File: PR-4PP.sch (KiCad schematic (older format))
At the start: 14 parts

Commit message: sch & pcb changes
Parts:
- added D1, D2, D3, D4: D_Small, Diode_SMD:D_SOD-123, symbol Device:D_Small
- added F1: 500mA, Fuse:Fuse_1206_3216Metric, symbol Device:Polyfuse
- added MX1, MX2, MX3: MX-NoLED, MX_Alps_Hybrid:MX-1U-NoLED, symbol MX_Alps_Hybrid:MX-NoLED
- added MX4: MX-NoLED, MX_Alps_Hybrid:MX-1U, symbol MX_Alps_Hybrid:MX-NoLED
- added USB1: Molex-0548190589, random-keyboard-parts:Molex-0548190589, symbol random-keyboard-parts:Molex-0548190589
- C1, C2, C3, C4, C5, C6, C7: renamed from C?; footprint (none) -> Capacitor_SMD:C_0805_2012Metric
- R1, R2, R3, R4: renamed from R?; footprint (none) -> Resistor_SMD:R_0805_2012Metric
- SW1: renamed from SW?; footprint (none) -> random-keyboard-parts:SKQG-1155865
- Y1: renamed from Y?; footprint (none) -> Crystal:Crystal_SMD_3225-4Pin_3.2x2.5mm
- gave numbers to parts that had none: 1
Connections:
- net +5V: now also F1.1
- net D+: now also USB1.3 (D+)
- net D-: now also USB1.4 (D-)
- net GND: now also USB1.1 (GND)
- new net: D1.2 (A), MX1.2 (ROW)
- new net: D3.2 (A), MX3.2 (ROW)
- new net: D2.2 (A), MX2.2 (ROW)
- new net: D4.2 (A), MX4.2 (ROW)
- new net COL0: MX1.1 (COL), MX3.1 (COL)
- new net COL1: MX2.1 (COL), MX4.1 (COL)
- new net ROW0: D1.1 (K), D2.1 (K)
- new net ROW1: D3.1 (K), D4.1 (K)
- new net VCC: F1.2, USB1.5 (VBUS)
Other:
- moved on the sheet: C1, C2, C3, C4, C5, C6, C7, R1, R2, R3, R4, SW1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

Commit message: finish pcb
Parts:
- renumbered C5 to C1, C7 to C3, C1 to C4, C2 to C5, C3 to C6, C4 to C7, R3 to R1, R1 to R3, C6 to c2
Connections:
- net COL0: now also U1.29 (PB5)
- net COL1: now also U1.28 (PB4)
- net ROW0: now also U1.27 (PD7)
- net ROW1: now also U1.30 (PB6)
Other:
- moved on the sheet: R4
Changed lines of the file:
@@
 L Device:R_Small R4
 U 1 1 6167D378
-P 5300 4850
-F 0 "R4" V 5104 4850 50  0000 C CNN
-F 1 "10k" V 5195 4850 50  0000 C CNN
-F 2 "Resistor_SMD:R_0805_2012Metric" H 5300 4850 50  0001 C CNN
-F 3 "~" H 5300 4850 50  0001 C CNN
-	1    5300 4850
-	0    1    1    0
-$EndComp
-Wire Wire Line
-	5200 4850 5000 4850
+P 5450 4850
+F 0 "R4" V 5254 4850 50  0000 C CNN
+F 1 "10k" V 5345 4850 50  0000 C CNN
+F 2 "Resistor_SMD:R_0805_2012Metric" H 5450 4850 50  0001 C CNN
+F 3 "~" H 5450 4850 50  0001 C CNN
+	1    5450 4850
+	0    1    1    0
+$EndComp
+Wire Wire Line
+	5350 4850 5000 4850
 $Comp
 L power:GND #PWR0103
@@
 $EndComp
 Wire Wire Line
-	5400 4850 5750 4850
+	5550 4850 5750 4850
 $Comp
 L Device:R_Small R2
@@
 $EndComp
 $Comp
-L Device:R_Small R1
+L Device:R_Small R3
 U 1 1 6167ECE6
 P 2900 3850
-F 0 "R1" V 2704 3850 50  0000 C CNN
+F 0 "R3" V 2704 3850 50  0000 C CNN
 F 1 "22" V 2795 3850 50  0000 C CNN
 F 2 "Resistor_SMD:R_0805_2012Metric" H 2900 3850 50  0001 C CNN
@@
 	3800 3750 3250 3750
 $Comp
-L Device:C_Small C7
+L Device:C_Small C3
 U 1 1 61680FED
 P 3150 4150
-F 0 "C7" H 3058 4104 50  0000 R CNN
+F 0 "C3" H 3058 4104 50  0000 R CNN
 F 1 "1uF" H 3058 4195 50  0000 R CNN
 F 2 "Capacitor_SMD:C_0805_2012Metric" H 3150 4150 50  0001 C CNN
@@
 	3150 4250 3150 4450
 $Comp
-L Device:C_Small C1
+L Device:C_Small C4
 U 1 1 616827A2
 P 1350 5100
-F 0 "C1" H 1442 5146 50  0000 L CNN
+F 0 "C4" H 1442 5146 50  0000 L CNN
 F 1 "0.1uF" H 1442 5055 50  0000 L CNN
 F 2 "Capacitor_SMD:C_0805_2012Metric" H 1350 5100 50  0001 C CNN
@@
 $EndComp
 $Comp
-L Device:C_Small C2
+L Device:C_Small C5
 U 1 1 61683F91
 P 1800 5100
-F 0 "C2" H 1892 5146 50  0000 L CNN
+F 0 "C5" H 1892 5146 50  0000 L CNN
 F 1 "0.1uF" H 1892 5055 50  0000 L CNN
 F 2 "Capacitor_SMD:C_0805_2012Metric" H 1800 5100 50  0001 C CNN
@@
 $EndComp
 $Comp
-L Device:C_Small C3
+L Device:C_Small C6
 U 1 1 616845F6
 P 2250 5100
-F 0 "C3" H 2342 5146 50  0000 L CNN
+F 0 "C6" H 2342 5146 50  0000 L CNN
 F 1 "0.1uF" H 2342 5055 50  0000 L CNN
 F 2 "Capacitor_SMD:C_0805_2012Metric" H 2250 5100 50  0001 C CNN
@@
 $EndComp
 $Comp
-L Device:C_Small C4
+L Device:C_Small C7
 U 1 1 61684895
 P 2700 5100
-F 0 "C4" H 2792 5146 50  0000 L CNN
+F 0 "C7" H 2792 5146 50  0000 L CNN
 F 1 "10uF" H 2792 5055 50  0000 L CNN
 F 2 "Capacitor_SMD:C_0805_2012Metric" H 2700 5100 50  0001 C CNN
@@
 	3800 3150 3200 3150
 $Comp
-L Device:C_Small C5
+L Device:C_Small C1
 U 1 1 61689DB9
 P 2750 2850
-F 0 "C5" V 2521 2850 50  0000 C CNN
+F 0 "C1" V 2521 2850 50  0000 C CNN
 F 1 "22pF" V 2612 2850 50  0000 C CNN
 F 2 "Capacitor_SMD:C_0805_2012Metric" H 2750 2850 50  0001 C CNN
@@
 $EndComp
 $Comp
-L Device:C_Small C6
+L Device:C_Small c2
 U 1 1 6168B87D
 P 2750 3250
-F 0 "C6" V 2521 3250 50  0000 C CNN
+F 0 "c2" V 2521 3250 50  0000 C CNN
 F 1 "22pF" V 2612 3250 50  0000 C CNN
 F 2 "Capacitor_SMD:C_0805_2012Metric" H 2750 3250 50  0001 C CNN
@@
 	3250 2700 3050 2700
 $Comp
-L Device:R_Small R3
+L Device:R_Small R1
 U 1 1 61694BD5
 P 3750 2450
-F 0 "R3" H 3809 2496 50  0000 L CNN
+F 0 "R1" H 3809 2496 50  0000 L CNN
 F 1 "10k" H 3809 2405 50  0000 L CNN
 F 2 "Resistor_SMD:R_0805_2012Metric" H 3750 2450 50  0001 C CNN
@@
 	7400 4850 8300 4850
 Wire Wire Line
-	2650 2850 2650 3250
-Wire Wire Line
-	2650 3250 2650 3400
-Connection ~ 2650 3250
-Wire Wire Line
 	2650 3400 3100 3400
 Wire Wire Line
@@
 	2850 2950 2850 2850
 Connection ~ 3200 2950
+Wire Wire Line
+	2650 2850 2650 3250
+Connection ~ 2650 3250
+Wire Wire Line
+	2650 3250 2650 3400
+Text GLabel 5000 4650 2    50   Input ~ 0
+ROW0
+Text GLabel 5000 3350 2    50   Input ~ 0
+ROW1
+Text GLabel 5000 3250 2    50   Input ~ 0
+COL0
+Text GLabel 5000 3150 2    50   Input ~ 0
+COL1
 $EndSCHEMATC

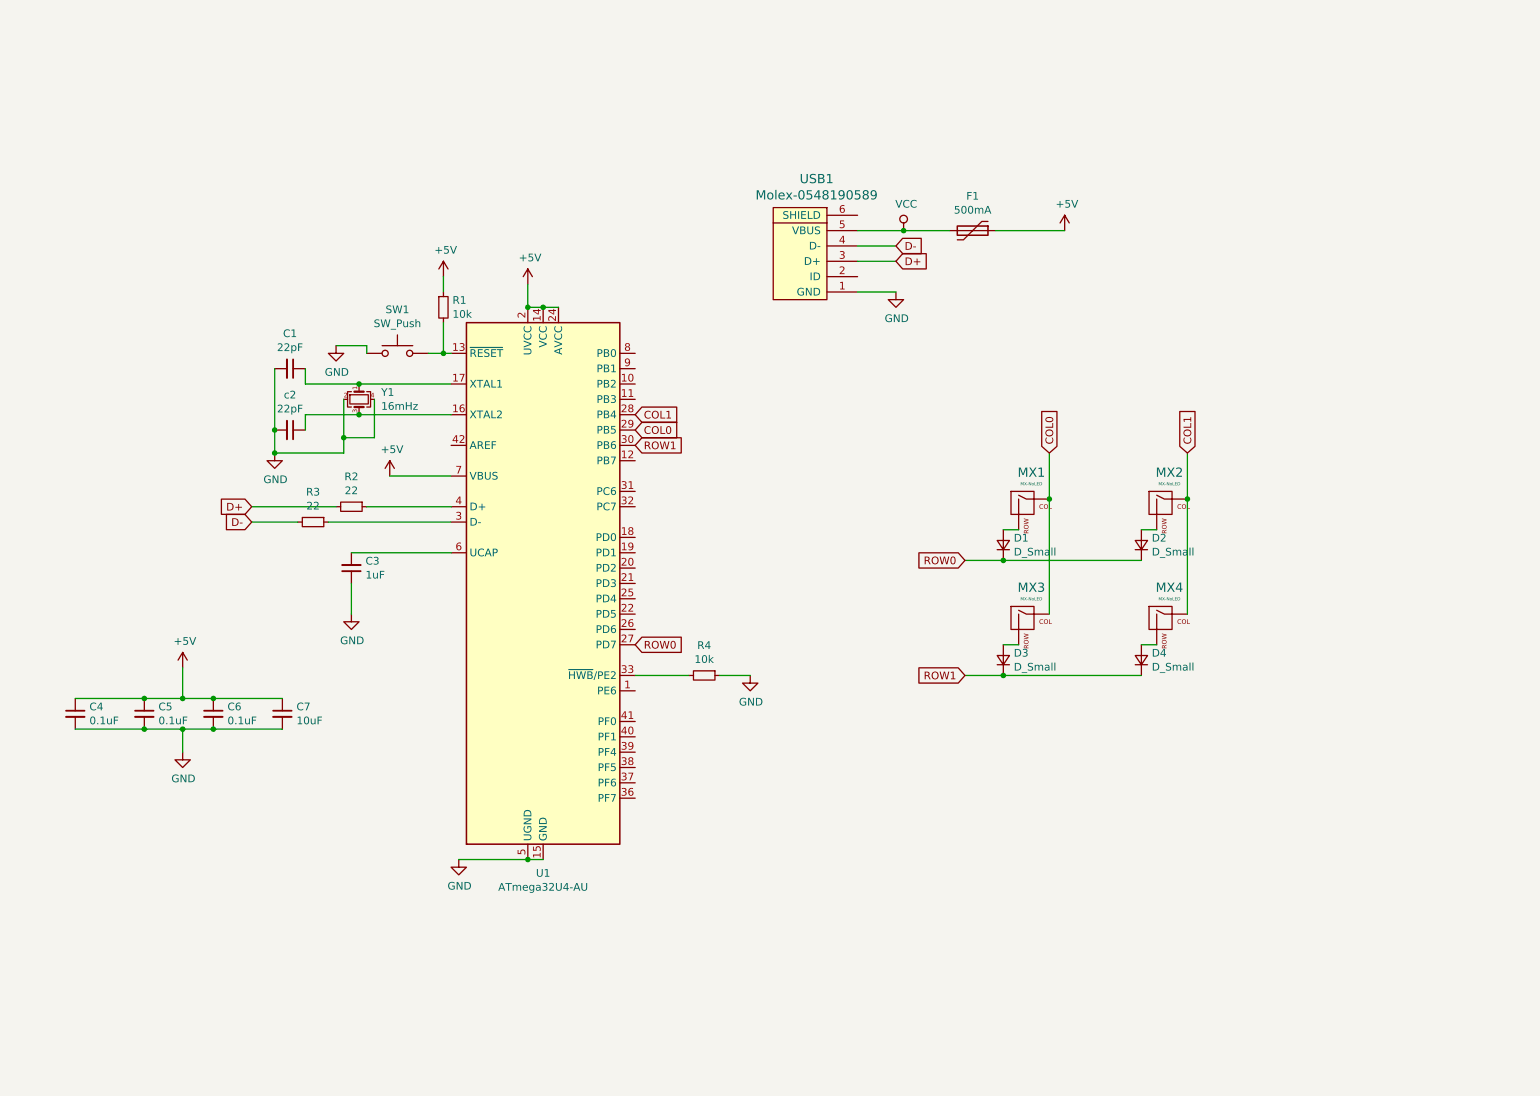
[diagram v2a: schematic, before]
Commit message: replace usb-mini-b with usb-c 2.0
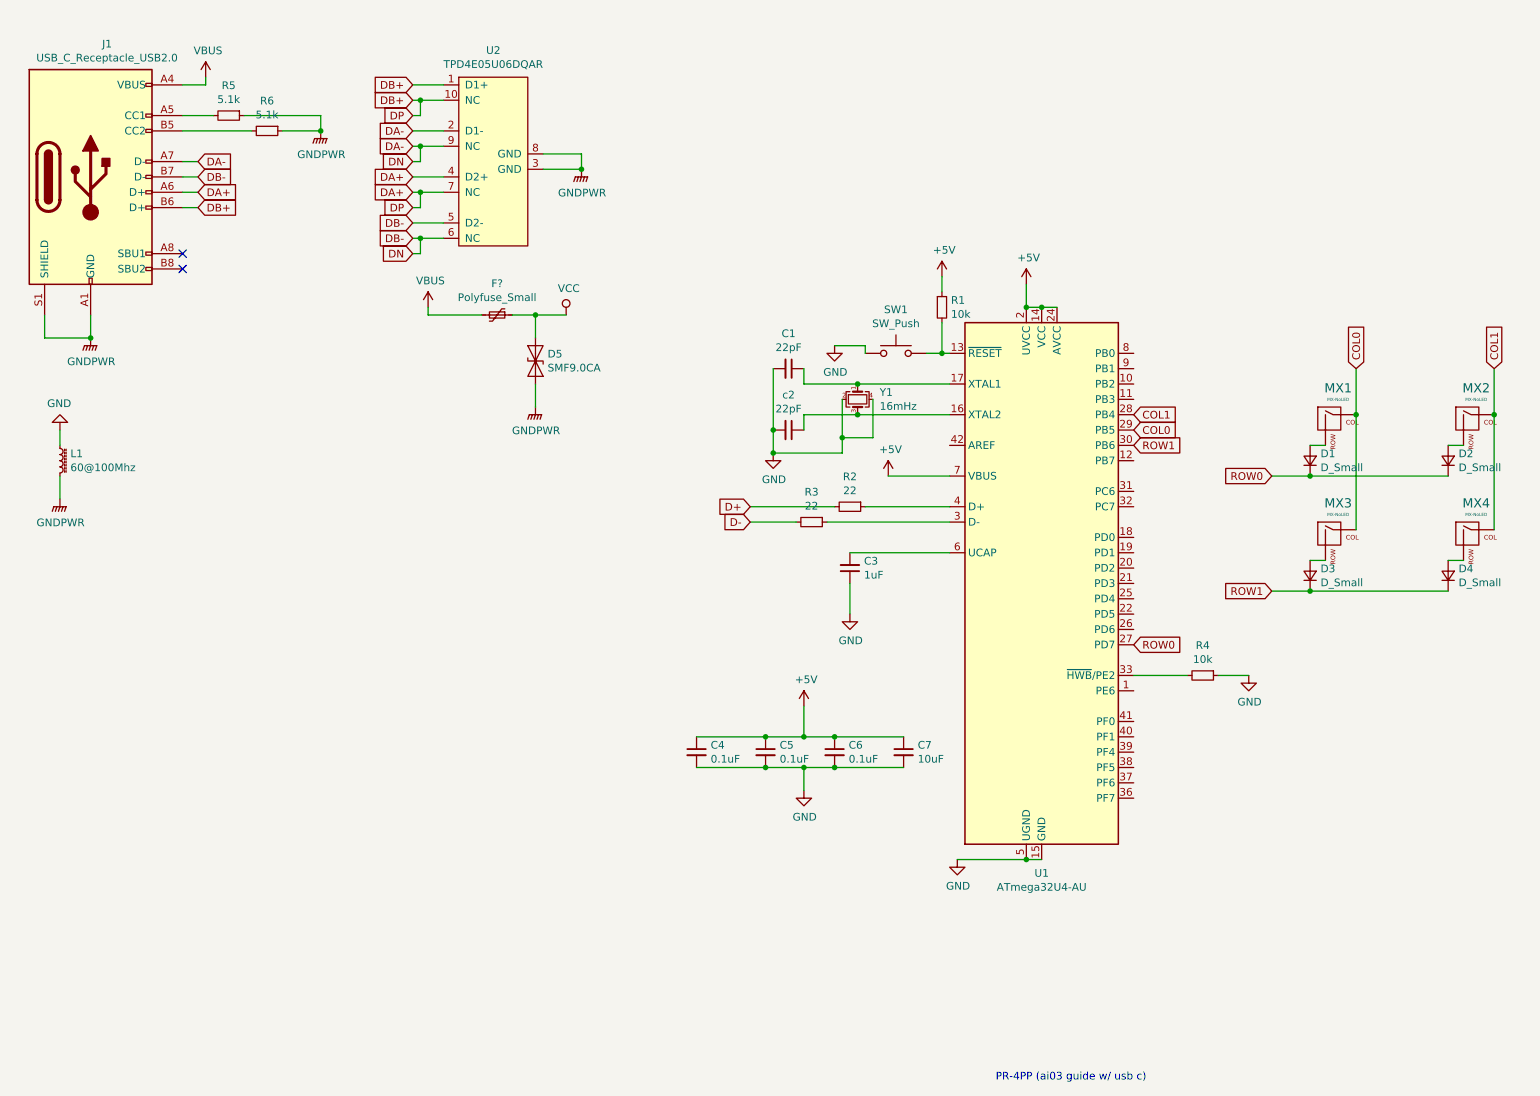
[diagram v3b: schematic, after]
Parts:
- removed F1: 500mA, Fuse:Fuse_1206_3216Metric, symbol Device:Polyfuse
- removed USB1: Molex-0548190589, random-keyboard-parts:Molex-0548190589, symbol random-keyboard-parts:Molex-0548190589
- added D5: SMF9.0CA, Diode_SMD:D_SOD-123, symbol Diode:1N630xCA
- added F?: Polyfuse_Small, symbol Device:Polyfuse_Small
- added J1: USB_C_Receptacle_USB2.0, symbol Connector:USB_C_Receptacle_USB2.0
- added L1: 60@100Mhz, symbol Device:L_Core_Ferrite_Small
- added R5, R6: 5.1k, symbol Device:R_Small
- added U2: TPD4E05U06DQAR, symbol random-keyboard-parts:TPD4E05U06DQAR
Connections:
- net GND: now also L1.1
- net VCC: now also D5.1 (A1), F?.1
- new net: J1.A5 (CC1), R5.2
- new net: J1.B5 (CC2), R6.2
- new net DA+: J1.A6 (D+), J1.B6 (D+), U2.1 (D1+), U2.10 (NC), U2.4 (D2+), U2.7 (NC)
- new net DA-: J1.A7 (D-), J1.B7 (D-), U2.2 (D1-), U2.5 (D2-), U2.6 (NC), U2.9 (NC)
- new net GNDPWR: D5.2 (A2), J1.A1 (GND), J1.A12 (GND), J1.B1 (GND), J1.B12 (GND), J1.S1 (SHIELD), L1.2, R5.1, R6.1, U2.3 (GND), U2.8 (GND)
- new net VBUS: F?.2, J1.A4 (VBUS), J1.A9 (VBUS), J1.B4 (VBUS), J1.B9 (VBUS)
- no-connect marks 0 -> 2
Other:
- note added: "PR-4PP (ai03 guide w/ usb c)"
- moved on the sheet: C1, C3, C4, C5, C6, C7, D1, D2, D3, D4, MX1, MX2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

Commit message: add reference
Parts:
- gave numbers to parts that had none: 1
- renumbered c2 to C2
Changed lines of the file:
@@
 $EndComp
 $Comp
-L Device:C_Small c2
+L Device:C_Small C2
 U 1 1 6168B87D
 P 6000 3250
-F 0 "c2" V 5771 3250 50  0000 C CNN
+F 0 "C2" V 5771 3250 50  0000 C CNN
 F 1 "22pF" V 5862 3250 50  0000 C CNN
 F 2 "Capacitor_SMD:C_0805_2012Metric" H 6000 3250 50  0001 C CNN
@@
 $EndComp
 $Comp
-L power:VBUS #PWR?
+L power:VBUS #PWR0111
 U 1 1 6170BDF8
 P 2200 950
-F 0 "#PWR?" H 2200 800 50  0001 C CNN
+F 0 "#PWR0111" H 2200 800 50  0001 C CNN
 F 1 "VBUS" H 2215 1123 50  0000 C CNN
 F 2 "" H 2200 950 50  0001 C CNN
@@
 	2050 1300 2500 1300
 $Comp
-L power:GNDPWR #PWR?
+L power:GNDPWR #PWR0112
 U 1 1 61717B5D
 P 2950 1300
-F 0 "#PWR?" H 2950 1100 50  0001 C CNN
+F 0 "#PWR0112" H 2950 1100 50  0001 C CNN
 F 1 "GNDPWR" H 2954 1146 50  0000 C CNN
 F 2 "" H 2950 1250 50  0001 C CNN
@@
 NoConn ~ 2050 2200
 $Comp
-L power:GNDPWR #PWR?
+L power:GNDPWR #PWR0113
 U 1 1 6171D868
 P 1450 2650
-F 0 "#PWR?" H 1450 2450 50  0001 C CNN
+F 0 "#PWR0113" H 1450 2450 50  0001 C CNN
 F 1 "GNDPWR" H 1454 2496 50  0000 C CNN
 F 2 "" H 1450 2600 50  0001 C CNN
@@
 $EndComp
 $Comp
-L power:GND #PWR?
+L power:GND #PWR0114
 U 1 1 6172D0C5
 P 1250 3250
-F 0 "#PWR?" H 1250 3000 50  0001 C CNN
+F 0 "#PWR0114" H 1250 3000 50  0001 C CNN
 F 1 "GND" H 1255 3077 50  0000 C CNN
 F 2 "" H 1250 3250 50  0001 C CNN
@@
 	1250 3250 1250 3350
 $Comp
-L power:GNDPWR #PWR?
+L power:GNDPWR #PWR0115
 U 1 1 6172F9F8
 P 1250 3700
-F 0 "#PWR?" H 1250 3500 50  0001 C CNN
+F 0 "#PWR0115" H 1250 3500 50  0001 C CNN
 F 1 "GNDPWR" H 1254 3546 50  0000 C CNN
 F 2 "" H 1250 3650 50  0001 C CNN
@@
 	3600 2000 3750 2000
 $Comp
-L power:GNDPWR #PWR?
+L power:GNDPWR #PWR0116
 U 1 1 61783B2B
 P 4650 1550
-F 0 "#PWR?" H 4650 1350 50  0001 C CNN
+F 0 "#PWR0116" H 4650 1350 50  0001 C CNN
 F 1 "GNDPWR" H 4654 1396 50  0000 C CNN
 F 2 "" H 4650 1500 50  0001 C CNN
@@
 Connection ~ 4650 1550
 $Comp
-L Device:Polyfuse_Small F?
+L Device:Polyfuse_Small F1
 U 1 1 6178F237
 P 4100 2500
-F 0 "F?" V 3895 2500 50  0000 C CNN
+F 0 "F1" V 3895 2500 50  0000 C CNN
 F 1 "Polyfuse_Small" V 3986 2500 50  0000 C CNN
 F 2 "" H 4150 2300 50  0001 L CNN
@@
 $EndComp
 $Comp
-L power:VBUS #PWR?
+L power:VBUS #PWR0117
 U 1 1 6179E139
 P 3650 2450
-F 0 "#PWR?" H 3650 2300 50  0001 C CNN
+F 0 "#PWR0117" H 3650 2300 50  0001 C CNN
 F 1 "VBUS" H 3665 2623 50  0000 C CNN
 F 2 "" H 3650 2450 50  0001 C CNN
@@
 	3650 2500 4000 2500
 $Comp
-L power:VCC #PWR?
+L power:VCC #PWR0118
 U 1 1 617A2075
 P 4550 2500
-F 0 "#PWR?" H 4550 2350 50  0001 C CNN
+F 0 "#PWR0118" H 4550 2350 50  0001 C CNN
 F 1 "VCC" H 4567 2673 50  0000 C CNN
 F 2 "" H 4550 2500 50  0001 C CNN
@@
 	4350 2500 4200 2500
 $Comp
-L power:GNDPWR #PWR?
+L power:GNDPWR #PWR0119
 U 1 1 617B1979
 P 4350 3100
-F 0 "#PWR?" H 4350 2900 50  0001 C CNN
+F 0 "#PWR0119" H 4350 2900 50  0001 C CNN
 F 1 "GNDPWR" H 4354 2946 50  0000 C CNN
 F 2 "" H 4350 3050 50  0001 C CNN

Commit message: replace esd for srv05-4 & add power flags
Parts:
- removed D5: SMF9.0CA, Diode_SMD:D_SOD-123, symbol Diode:1N630xCA
- removed F1: Polyfuse_Small, symbol Device:Polyfuse_Small
- removed U2: TPD4E05U06DQAR, symbol random-keyboard-parts:TPD4E05U06DQAR
- added F1: 750mA, symbol Device:Fuse_Small
- added U3: SRV05-4, Package_TO_SOT_SMD:SOT-23-6, symbol Power_Protection:SRV05-4
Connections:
- net DA+ is gone; now on net D+: J1.A6 (D+), J1.B6 (D+)
- net DA- is gone; now on net D-: J1.A7 (D-), J1.B7 (D-)
- net +5V: now also F1.2, U3.5 (VP)
- net D+: now also U3.1 (IO1)
- net D-: now also U3.6 (IO4)
- net GNDPWR: now also U3.2 (VN)
- net VBUS: now also F1.1
- no-connect marks 2 -> 26

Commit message: make power flags obvious
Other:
- moved on the sheet: F1, J1, L1, R5, R6, U3

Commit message: add footprints
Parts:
- D1, D2, D3, D4: footprint Diode_SMD:D_SOD-123 -> random-keyboard-parts:D_SOD-123-Pretty
- F1: value 750mA -> 500mA; footprint (none) -> Fuse:Fuse_1206_3216Metric_Pad1.42x1.75mm_HandSolder
- L1: footprint (none) -> Inductor_SMD:L_1206_3216Metric_Pad1.42x1.75mm_HandSolder
- R5, R6: footprint (none) -> Capacitor_SMD:C_0805_2012Metric_Pad1.15x1.40mm_HandSolder
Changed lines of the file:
@@
 F 0 "D3" V 9446 4132 50  0000 R CNN
 F 1 "D_Small" V 9355 4132 50  0000 R CNN
-F 2 "Diode_SMD:D_SOD-123" V 9400 4200 50  0001 C CNN
+F 2 "random-keyboard-parts:D_SOD-123-Pretty" V 9400 4200 50  0001 C CNN
 F 3 "~" V 9400 4200 50  0001 C CNN
 	1    9400 4200
@@
 F 0 "D2" V 10346 3382 50  0000 R CNN
 F 1 "D_Small" V 10255 3382 50  0000 R CNN
-F 2 "Diode_SMD:D_SOD-123" V 10300 3450 50  0001 C CNN
+F 2 "random-keyboard-parts:D_SOD-123-Pretty" V 10300 3450 50  0001 C CNN
 F 3 "~" V 10300 3450 50  0001 C CNN
 	1    10300 3450
@@
 F 0 "D4" V 10346 4132 50  0000 R CNN
 F 1 "D_Small" V 10255 4132 50  0000 R CNN
-F 2 "Diode_SMD:D_SOD-123" V 10300 4200 50  0001 C CNN
+F 2 "random-keyboard-parts:D_SOD-123-Pretty" V 10300 4200 50  0001 C CNN
 F 3 "~" V 10300 4200 50  0001 C CNN
 	1    10300 4200
@@
 F 0 "D1" V 9446 3382 50  0000 R CNN
 F 1 "D_Small" V 9355 3382 50  0000 R CNN
-F 2 "Diode_SMD:D_SOD-123" V 9400 3450 50  0001 C CNN
+F 2 "random-keyboard-parts:D_SOD-123-Pretty" V 9400 3450 50  0001 C CNN
 F 3 "~" V 9400 3450 50  0001 C CNN
 	1    9400 3450
@@
 F 0 "R5" V 2154 1600 50  0000 C CNN
 F 1 "5.1k" V 2245 1600 50  0000 C CNN
-F 2 "" H 2350 1600 50  0001 C CNN
+F 2 "Capacitor_SMD:C_0805_2012Metric_Pad1.15x1.40mm_HandSolder" H 2350 1600 50  0001 C CNN
 F 3 "~" H 2350 1600 50  0001 C CNN
 	1    2350 1600
@@
 F 0 "R6" V 2404 1700 50  0000 C CNN
 F 1 "5.1k" V 2495 1700 50  0000 C CNN
-F 2 "" H 2600 1700 50  0001 C CNN
+F 2 "Capacitor_SMD:C_0805_2012Metric_Pad1.15x1.40mm_HandSolder" H 2600 1700 50  0001 C CNN
 F 3 "~" H 2600 1700 50  0001 C CNN
 	1    2600 1700
@@
 F 0 "L1" H 1318 3896 50  0000 L CNN
 F 1 "60@100Mhz" H 1318 3805 50  0000 L CNN
-F 2 "" H 1250 3850 50  0001 C CNN
+F 2 "Inductor_SMD:L_1206_3216Metric_Pad1.42x1.75mm_HandSolder" H 1250 3850 50  0001 C CNN
 F 3 "~" H 1250 3850 50  0001 C CNN
 	1    1250 3850
@@
 P 3950 1550
 F 0 "F1" H 3950 1735 50  0000 C CNN
-F 1 "750mA" H 3950 1644 50  0000 C CNN
-F 2 "" H 3950 1550 50  0001 C CNN
+F 1 "500mA" H 3950 1644 50  0000 C CNN
+F 2 "Fuse:Fuse_1206_3216Metric_Pad1.42x1.75mm_HandSolder" H 3950 1550 50  0001 C CNN
 F 3 "~" H 3950 1550 50  0001 C CNN
 	1    3950 1550
